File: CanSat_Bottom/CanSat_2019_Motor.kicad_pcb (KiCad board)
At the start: 2 copper layers, 65 x 65 mm, 32 parts, among them J1 Conn_01x12_Female, U1 DS18B20U, U2 DRV8838, U3 DS18B20U, U4 MAG3110, U5 MPU-9250

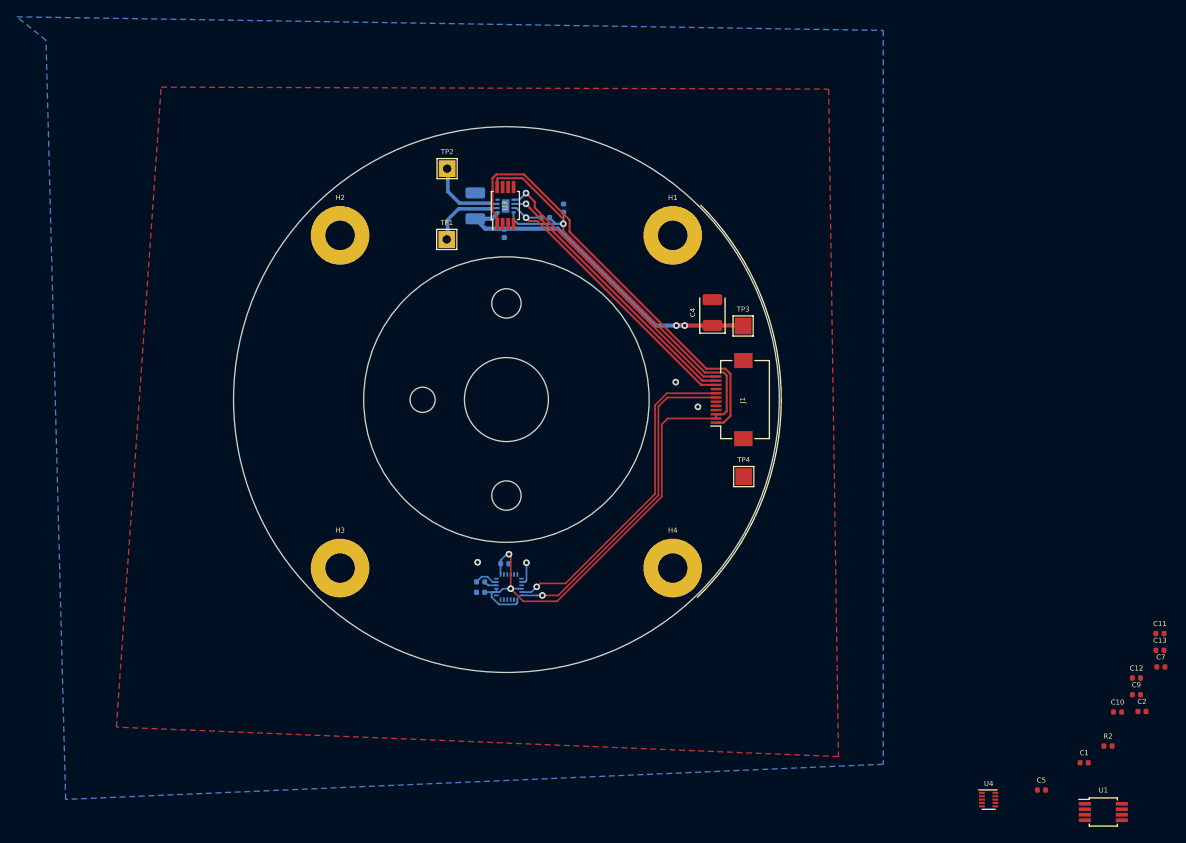
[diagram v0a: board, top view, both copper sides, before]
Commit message: Added OneWire Header and finished bottom PCB design
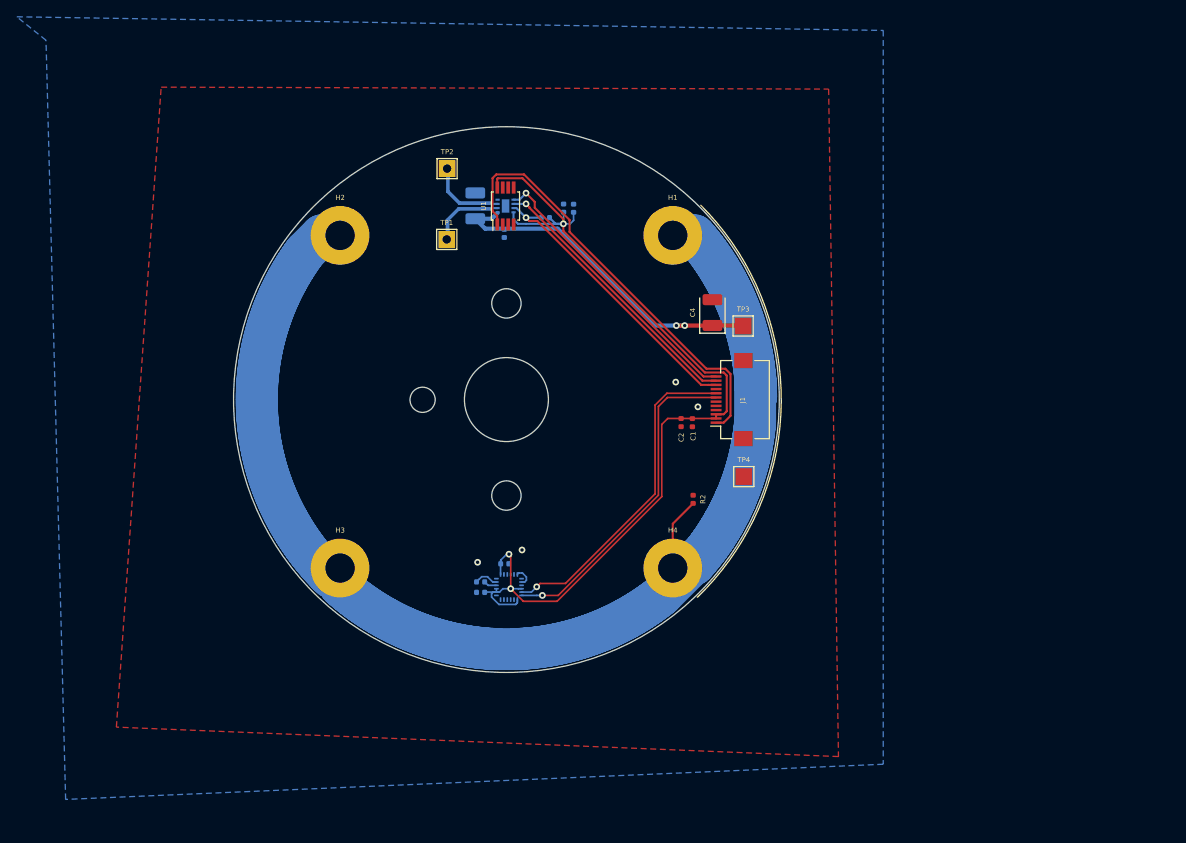
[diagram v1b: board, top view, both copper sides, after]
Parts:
- removed C10, C11, C9: 100n, Capacitor_SMD:C_0402_1005Metric
- removed the C12 at (202.0, 109.4)
- removed the C13 at (204.8, 106.1)
- removed the C7 at (204.9, 108.0)
- removed U3: DS18B20U, Package_SO:MSOP-8_3x3mm_P0.65mm
- removed the U4 at (184.4, 123.8)
- C5: moved to B.Cu
- moved U1 101.4 mm to (126.9, 53.1), turned to 90 degrees
- moved C5 88.9 mm to (135.0, 53.4), turned to 90 degrees
- moved C2 64.8 mm to (147.8, 78.9), turned to 270 degrees
- moved C1 61.8 mm to (149.1, 79.0), turned to 270 degrees
- moved R2 57.5 mm to (149.2, 88.1), turned to 270 degrees
- renumbered C14 to C12, C15 to C13, C16 to C14, C8 to C7, U5 to U4
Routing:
- net Net-(H1-Pad1): track 0.00 -> 175.8 mm
- net +3V3: track 111.7 -> 114.0 mm
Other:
- outline, holes or cut-outs redrawn

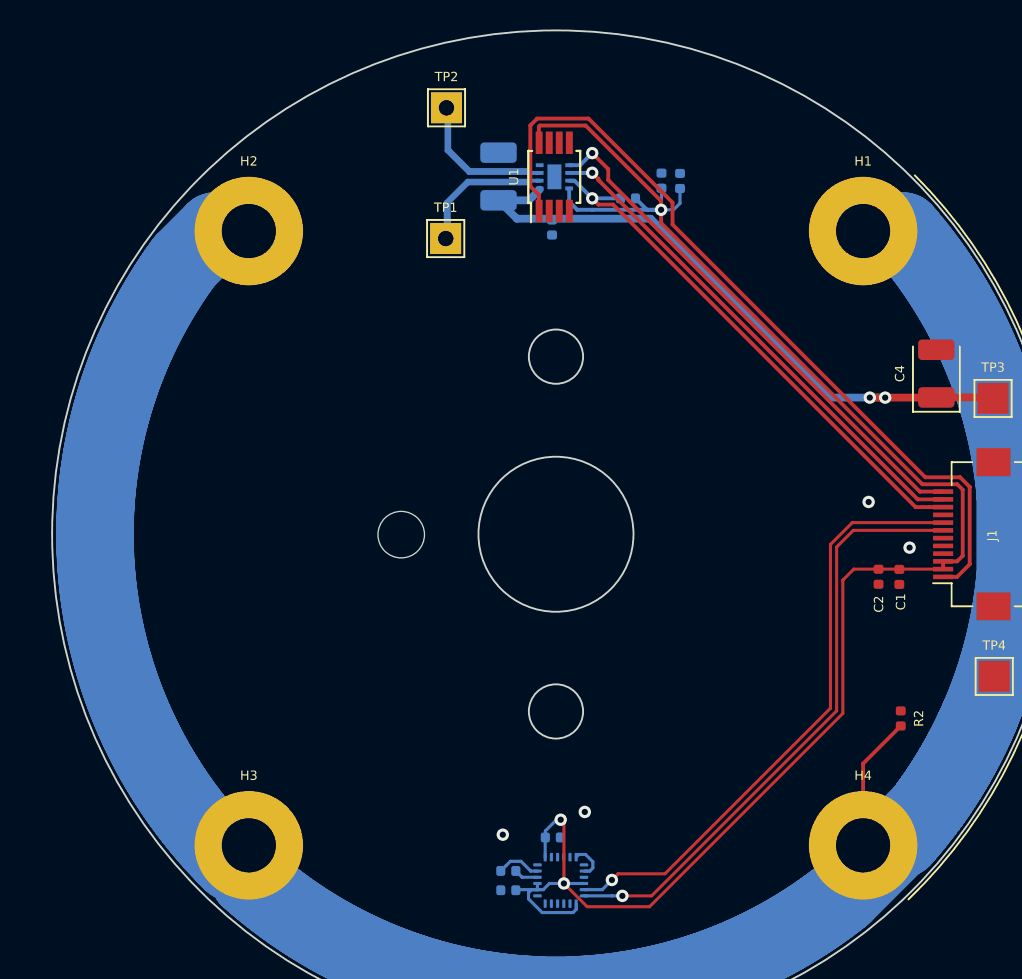
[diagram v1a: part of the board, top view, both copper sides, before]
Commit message: Added vias
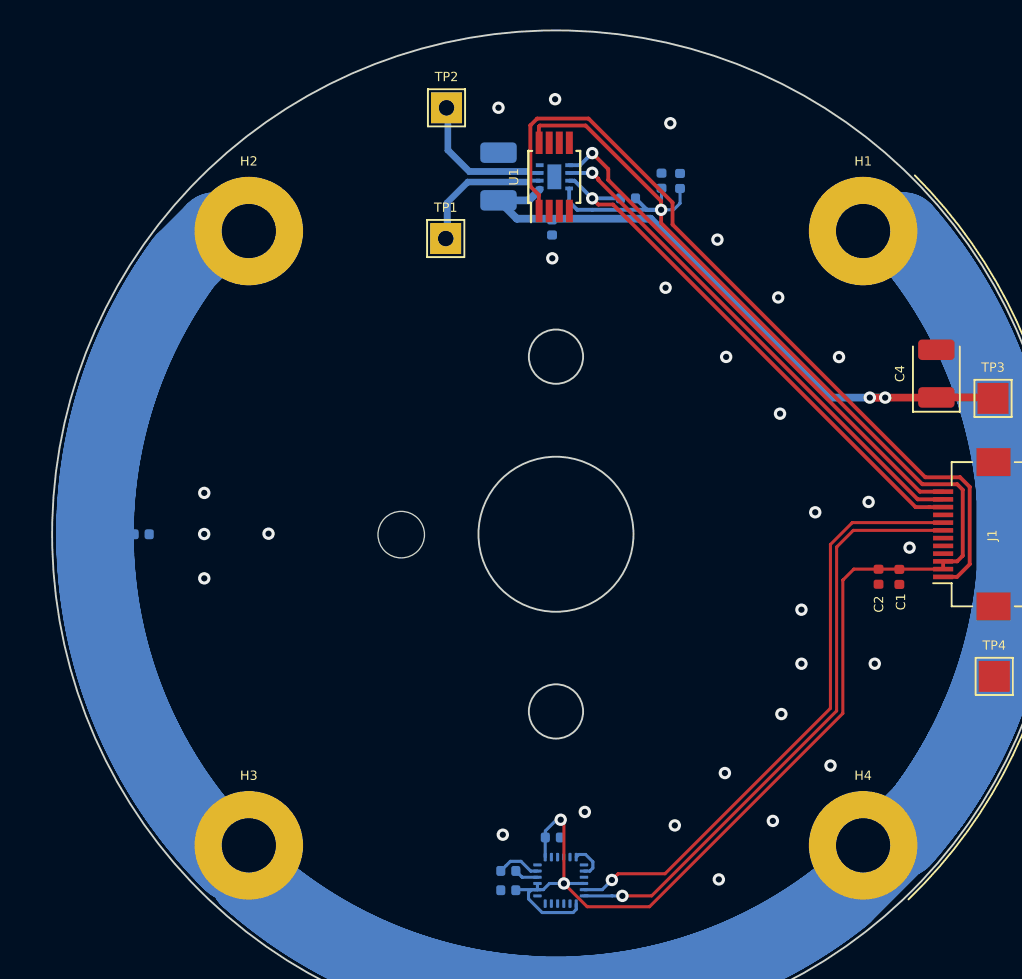
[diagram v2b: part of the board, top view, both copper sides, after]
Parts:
- R2: moved to B.Cu
- moved R2 50.4 mm to (100.3, 76.2), turned to 180 degrees
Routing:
- net Net-(H1-Pad1): track 175.8 -> 169.8 mm
- net GND: vias 4 -> 28
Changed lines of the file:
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@@
     (thickness 1.6)
     (drawings 8)
-    (tracks 595)
+    (tracks 619)
     (zones 0)
     (modules 24)
@@
       (net 11 "Net-(TP1-Pad1)"))
   )
-  (module Resistor_SMD:R_0402_1005Metric (layer F.Cu)
-    (at 149.24024 88.07944 270)
+  (module Resistor_SMD:R_0402_1005Metric (layer B.Cu)
+    (at 100.27412 76.2 180)
     (descr "Resistor SMD 0402 (1005 Metric), square (rectangular) end terminal, IPC_7351 nominal, (Body size source: http://www.tortai-tech.com/upload/download/2011102023233369053.pdf), generated with kicad-footprint-generator")
     (tags resistor)
     (attr smd)
-    (fp_text reference R2 (at 0 -1.17 270) (layer F.SilkS)
-      (effects (font (size 0.6 0.6) (thickness 0.1)))
-    )
-    (fp_text value 1M (at 0 1.17 270) (layer F.Fab)
-      (effects (font (size 1 1) (thickness 0.15)))
-    )
-    (fp_text user %R (at 0 0 270) (layer F.Fab)
-      (effects (font (size 0.6 0.6) (thickness 0.1)))
-    )
-    (fp_line (start 0.93 0.47) (end -0.93 0.47) (layer F.CrtYd) (width 0.05))
-    (fp_line (start 0.93 -0.47) (end 0.93 0.47) (layer F.CrtYd) (width 0.05))
-    (fp_line (start -0.93 -0.47) (end 0.93 -0.47) (layer F.CrtYd) (width 0.05))
-    (fp_line (start -0.93 0.47) (end -0.93 -0.47) (layer F.CrtYd) (width 0.05))
-    (fp_line (start 0.5 0.25) (end -0.5 0.25) (layer F.Fab) (width 0.1))
-    (fp_line (start 0.5 -0.25) (end 0.5 0.25) (layer F.Fab) (width 0.1))
-    (fp_line (start -0.5 -0.25) (end 0.5 -0.25) (layer F.Fab) (width 0.1))
-    (fp_line (start -0.5 0.25) (end -0.5 -0.25) (layer F.Fab) (width 0.1))
-    (pad 2 smd roundrect (at 0.485 0 270) (size 0.59 0.64) (layers F.Cu F.Paste F.Mask) (roundrect_rratio 0.25)
+    (fp_text reference R2 (at 0 1.17 180) (layer B.SilkS)
+      (effects (font (size 0.6 0.6) (thickness 0.1)) (justify mirror))
+    )
+    (fp_text value 1M (at 0 -1.17 180) (layer B.Fab)
+      (effects (font (size 1 1) (thickness 0.15)) (justify mirror))
+    )
+    (fp_text user %R (at 0 0 180) (layer B.Fab)
+      (effects (font (size 0.6 0.6) (thickness 0.1)) (justify mirror))
+    )
+    (fp_line (start 0.93 -0.47) (end -0.93 -0.47) (layer B.CrtYd) (width 0.05))
+    (fp_line (start 0.93 0.47) (end 0.93 -0.47) (layer B.CrtYd) (width 0.05))
+    (fp_line (start -0.93 0.47) (end 0.93 0.47) (layer B.CrtYd) (width 0.05))
+    (fp_line (start -0.93 -0.47) (end -0.93 0.47) (layer B.CrtYd) (width 0.05))
+    (fp_line (start 0.5 -0.25) (end -0.5 -0.25) (layer B.Fab) (width 0.1))
+    (fp_line (start 0.5 0.25) (end 0.5 -0.25) (layer B.Fab) (width 0.1))
+    (fp_line (start -0.5 0.25) (end 0.5 0.25) (layer B.Fab) (width 0.1))
+    (fp_line (start -0.5 -0.25) (end -0.5 0.25) (layer B.Fab) (width 0.1))
+    (pad 2 smd roundrect (at 0.485 0 180) (size 0.59 0.64) (layers B.Cu B.Paste B.Mask) (roundrect_rratio 0.25)
       (net 4 "Net-(H1-Pad1)"))
-    (pad 1 smd roundrect (at -0.485 0 270) (size 0.59 0.64) (layers F.Cu F.Paste F.Mask) (roundrect_rratio 0.25)
+    (pad 1 smd roundrect (at -0.485 0 180) (size 0.59 0.64) (layers B.Cu B.Paste B.Mask) (roundrect_rratio 0.25)
       (net 1 GND))
     (model ${KISYS3DMOD}/Resistor_SMD.3dshapes/R_0402_1005Metric.wrl
@@
   (segment (start 129.37981 97.33162) (end 129.37981 97.72659) (width 0.2) (layer B.Cu) (net 1))
   (segment (start 128.3048 97.0266) (end 128.47551 96.85589) (width 0.2) (layer B.Cu) (net 1))
+  (via (at 104.30764 76.18476) (size 0.8) (drill 0.4) (layers F.Cu B.Cu) (net 1))
+  (via (at 108.458 76.16444) (size 0.8) (drill 0.4) (layers F.Cu B.Cu) (net 1))
+  (via (at 104.31272 73.533) (size 0.8) (drill 0.4) (layers F.Cu B.Cu) (net 1))
+  (via (at 104.31272 79.0448) (size 0.8) (drill 0.4) (layers F.Cu B.Cu) (net 1))
+  (via (at 123.2916 48.68672) (size 0.8) (drill 0.4) (layers F.Cu B.Cu) (net 1))
+  (via (at 126.94412 48.13808) (size 0.8) (drill 0.4) (layers F.Cu B.Cu) (net 1))
+  (via (at 126.76124 58.39968) (size 0.8) (drill 0.4) (layers F.Cu B.Cu) (net 1))
+  (via (at 134.37616 49.68748) (size 0.8) (drill 0.4) (layers F.Cu B.Cu) (net 1))
+  (via (at 134.07136 60.2996) (size 0.8) (drill 0.4) (layers F.Cu B.Cu) (net 1))
+  (via (at 137.414 57.19572) (size 0.8) (drill 0.4) (layers F.Cu B.Cu) (net 1))
+  (via (at 137.97788 64.75984) (size 0.8) (drill 0.4) (layers F.Cu B.Cu) (net 1))
+  (via (at 141.33576 60.92444) (size 0.8) (drill 0.4) (layers F.Cu B.Cu) (net 1))
+  (via (at 141.4526 68.42252) (size 0.8) (drill 0.4) (layers F.Cu B.Cu) (net 1))
+  (via (at 145.25752 64.77) (size 0.8) (drill 0.4) (layers F.Cu B.Cu) (net 1))
+  (via (at 137.50544 98.46564) (size 0.8) (drill 0.4) (layers F.Cu B.Cu) (net 1))
+  (via (at 134.66572 94.98076) (size 0.8) (drill 0.4) (layers F.Cu B.Cu) (net 1))
+  (via (at 137.8966 91.60256) (size 0.8) (drill 0.4) (layers F.Cu B.Cu) (net 1))
+  (via (at 140.99032 94.6912) (size 0.8) (drill 0.4) (layers F.Cu B.Cu) (net 1))
+  (via (at 144.70888 91.11996) (size 0.8) (drill 0.4) (layers F.Cu B.Cu) (net 1))
+  (via (at 141.53896 87.79764) (size 0.8) (drill 0.4) (layers F.Cu B.Cu) (net 1))
+  (via (at 142.83436 84.55152) (size 0.8) (drill 0.4) (layers F.Cu B.Cu) (net 1))
+  (via (at 147.56384 84.55152) (size 0.8) (drill 0.4) (layers F.Cu B.Cu) (net 1))
+  (via (at 142.83436 81.06664) (size 0.8) (drill 0.4) (layers F.Cu B.Cu) (net 1))
+  (via (at 143.72336 74.78268) (size 0.8) (drill 0.4) (layers F.Cu B.Cu) (net 1))
   (via (at 133.7818 55.2704) (size 0.8) (drill 0.4) (layers F.Cu B.Cu) (net 2))
   (segment (start 127.8484 53.8932) (end 127.8484 54.7472) (width 0.25) (layer B.Cu) (net 2))
@@
   (segment (start 151.739344 92.705434) (end 151.920996 92.429862) (width 5) (layer B.Cu) (net 4))
   (segment (start 151.366833 93.250569) (end 151.554559 92.979097) (width 5) (layer B.Cu) (net 4))
-  (segment (start 146.812 90.99268) (end 149.24024 88.56444) (width 0.25) (layer F.Cu) (net 4))
-  (segment (start 146.812 96.266) (end 146.812 90.99268) (width 0.25) (layer F.Cu) (net 4))
-  (segment (start 124.8188 98.3266) (end 125.8048 98.3266) (width 0.2) (layer B.Cu) (net 18))
-  (segment (start 124.4092 97.917) (end 124.8188 98.3266) (width 0.2) (layer B.Cu) (net 18))
+  (segment (start 97.591995 76.2) (end 97.261883 76.530112) (width 0.25) (layer B.Cu) (net 4))
+  (segment (start 99.78912 76.2) (end 97.591995 76.2) (width 0.25) (layer B.Cu) (net 4))
   (via (at 129.3368 51.6128) (size 0.8) (drill 0.4) (layers F.Cu B.Cu) (net 5))
   (segment (start 128.5564 52.3932) (end 129.3368 51.6128) (width 0.25) (layer B.Cu) (net 5))
@@
   (segment (start 120.1166 51.3842) (end 121.4374 52.705) (width 0.25) (layer B.Cu) (net 12))
   (segment (start 121.4374 52.705) (end 125.222 52.705) (width 0.25) (layer B.Cu) (net 12))
+  (segment (start 124.8188 98.3266) (end 125.8048 98.3266) (width 0.2) (layer B.Cu) (net 18))
+  (segment (start 124.4092 97.917) (end 124.8188 98.3266) (width 0.2) (layer B.Cu) (net 18))
   (zone (net 1) (net_name GND) (layer F.Cu) (hatch edge 0.508)
     (connect_pads (clearance 0.2))
